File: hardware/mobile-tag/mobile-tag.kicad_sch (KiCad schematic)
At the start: 21 parts, among them J1 SWD_Cable_Connector, J2 USB_B_Micro, U1 DWM1001

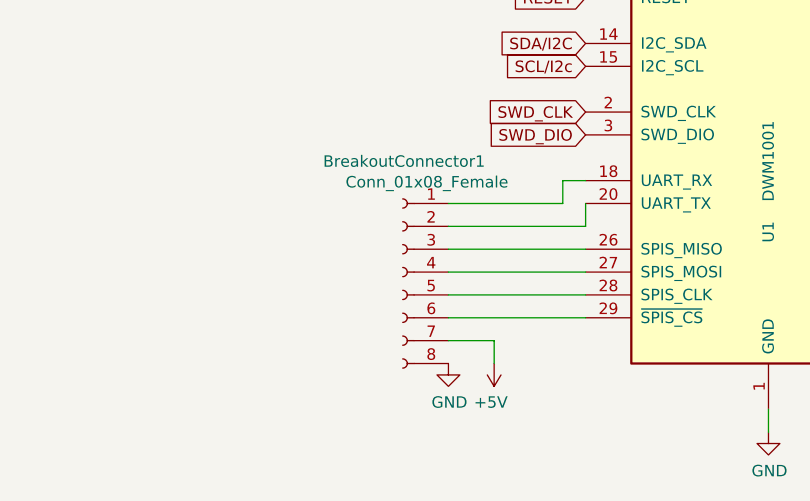
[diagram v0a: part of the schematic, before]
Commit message: wip: move things around
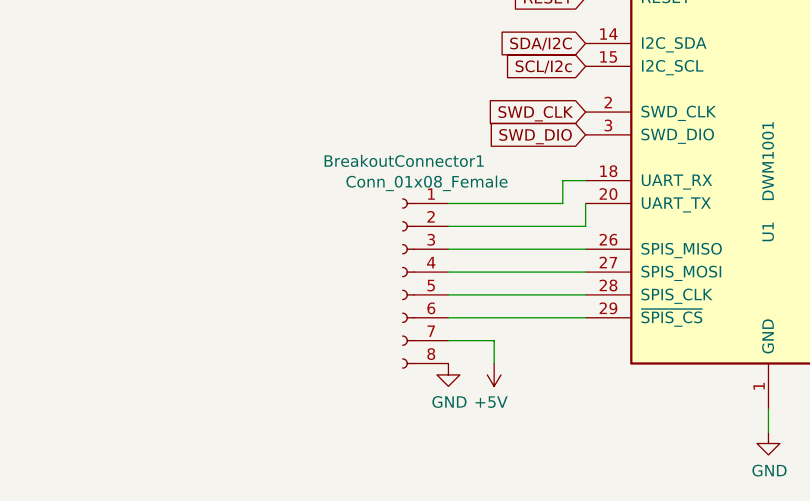
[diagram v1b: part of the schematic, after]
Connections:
- net ~RESET renamed ~{RESET}
